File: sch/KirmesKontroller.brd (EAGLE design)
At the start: 100 x 80 mm, 24 parts, among them IC1 R-78E05-1.0, IC2 YB-ESP32-S3-AMP-V2, IC3 ULN2803, J1 MPE 087-1-003, X2 DG240 2,54-8, X4 DG240 2,54-8, X5 DG240 2,54-2, X6 DG240 2,54-2

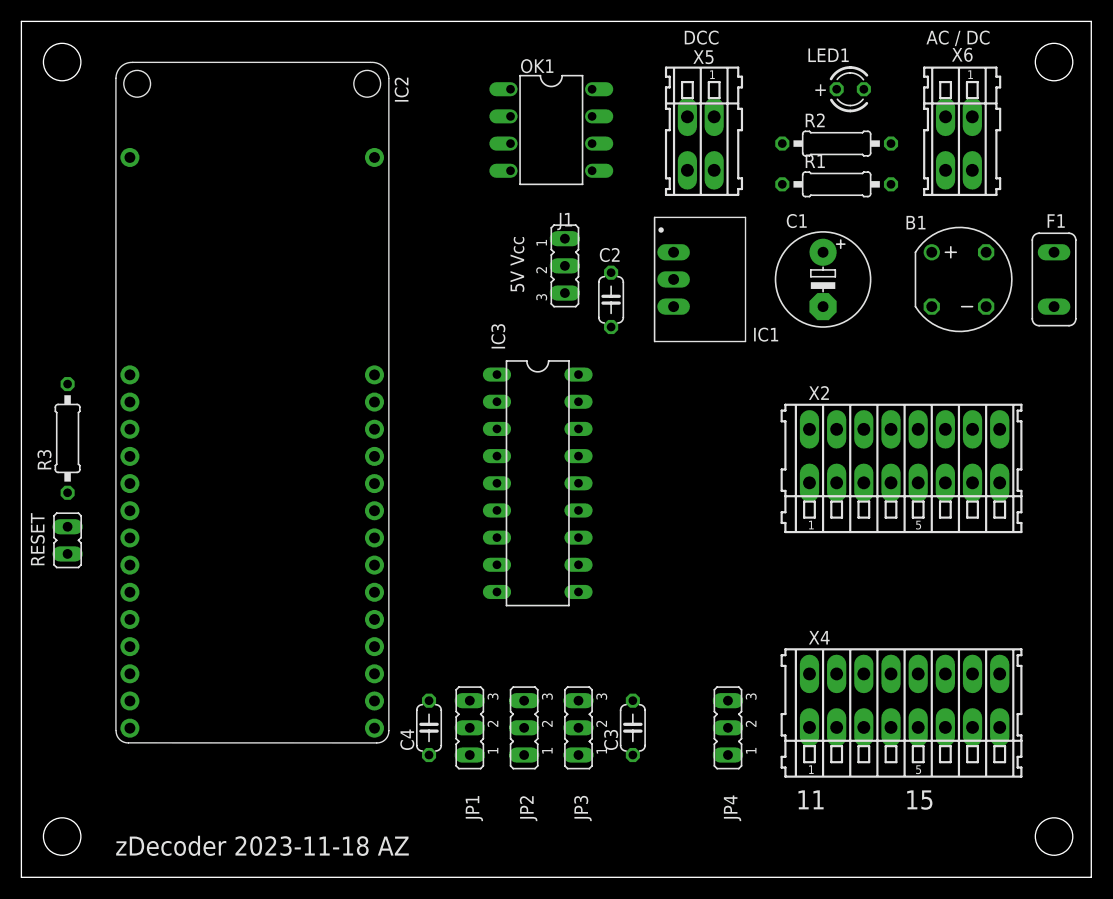
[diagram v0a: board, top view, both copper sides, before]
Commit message: fix: indexes changed
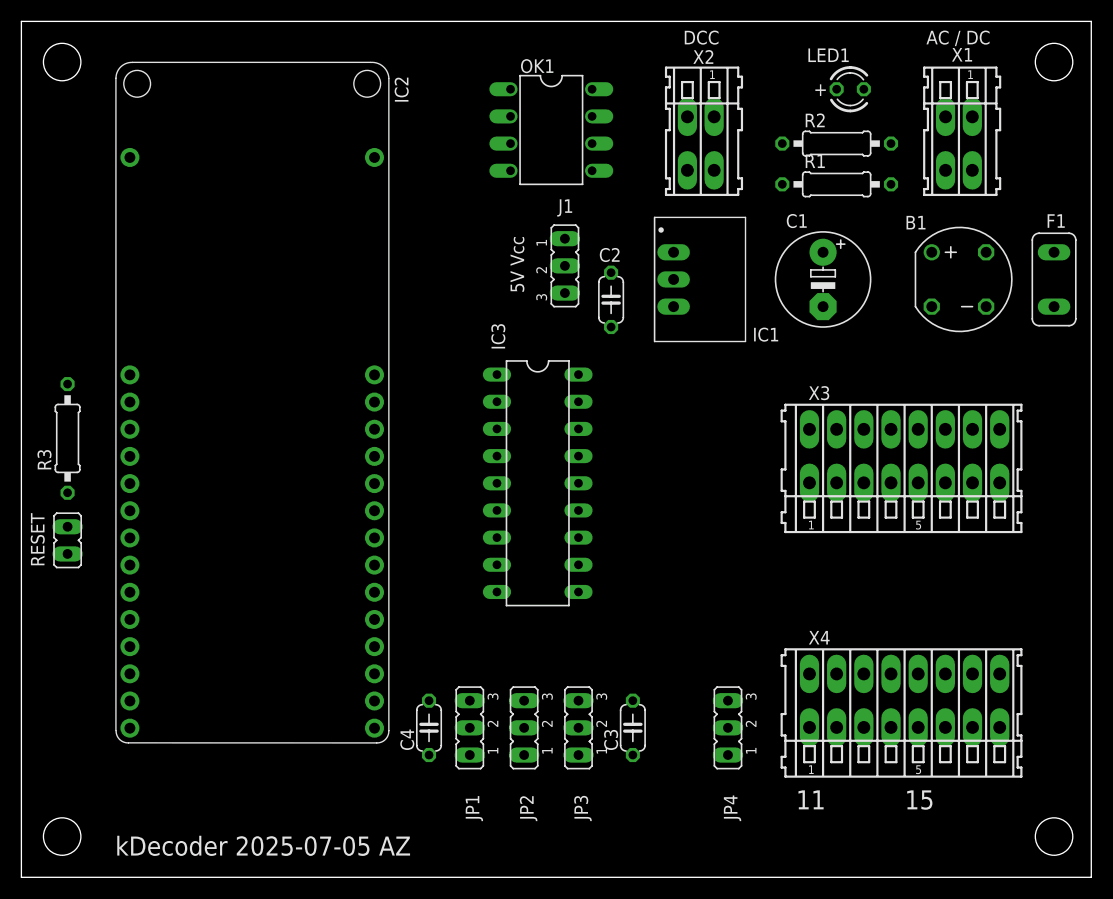
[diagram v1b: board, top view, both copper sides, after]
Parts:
- removed X5: DG240 2,54-2, con-wago255:233-202
- added X3: DG240 2,54-8, con-wago255:233-508
- X2: value DG240 2,54-8 -> DG240 2,54-2; device con-wago255:233-508 -> con-wago255:233-202
- moved X2 34.9 mm to (63.5, 68.6), turned to 180 degrees
- renumbered X6 to X1
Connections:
- net N$11: now also X2.A2; no longer X5.A2
- net N$12: now also X3.A4; no longer X2.A4
- net N$13: now also X3.A3; no longer X2.A3
- net N$14: now also X3.A2; no longer X2.A2
- net N$2: now also X3.A1; no longer X2.A1
- net N$23: now also X3.A8; no longer X2.A8
- net N$4: now also X3.A7; no longer X2.A7
- net N$7: now also X3.A6; no longer X2.A6
- net N$8: now also X3.A5; no longer X2.A5
- net N$9: now also X2.A1; no longer X5.A1
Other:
- board text added: "kDecoder 2025-07-05 AZ"
- board text removed: "zDecoder 2023-11-18 AZ"
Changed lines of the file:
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@@
 <dimension x1="100" y1="80" x2="0" y2="80" x3="50" y3="83.82" textsize="1.778" layer="1"/>
 <dimension x1="0" y1="80" x2="0" y2="0" x3="-3.81" y3="40" textsize="1.778" layer="1"/>
-<text x="8.763" y="2.032" size="1.778" layer="25">zDecoder 2023-11-18 AZ</text>
+<text x="8.763" y="2.032" size="1.778" layer="25">kDecoder 2025-07-05 AZ</text>
 <text x="46.99" y="57.15" size="1.27" layer="25" rot="R90">Vcc</text>
 <text x="46.99" y="54.61" size="1.27" layer="25" rot="R90">5V</text>
@@
 <attribute name="VALUE" x="73.9394" y="67.945" size="1.27" layer="27" ratio="10"/>
 </element>
-<element name="X2" library="con-wago255" library_urn="urn:adsk.eagle:library:198" package="233-508" package3d_urn="urn:adsk.eagle:package:10938/1" value="DG240 2,54-8" x="82.55" y="39.37" smashed="yes">
+<element name="X3" library="con-wago255" library_urn="urn:adsk.eagle:library:198" package="233-508" package3d_urn="urn:adsk.eagle:package:10938/1" value="DG240 2,54-8" x="82.55" y="39.37" smashed="yes">
 <attribute name="MF" value="Wago Corporation" x="106.68" y="-20.32" size="1.778" layer="27" display="off"/>
 <attribute name="MPN" value="0233-0508" x="106.68" y="-20.32" size="1.778" layer="27" display="off"/>
@@
 <attribute name="VALUE" x="82.81" y="21.76" size="1.27" layer="27"/>
 </element>
-<element name="X5" library="con-wago255" library_urn="urn:adsk.eagle:library:198" package="233-202" package3d_urn="urn:adsk.eagle:package:10884/1" value="DG240 2,54-2" x="63.5" y="68.58" smashed="yes" rot="R180">
+<element name="X2" library="con-wago255" library_urn="urn:adsk.eagle:library:198" package="233-202" package3d_urn="urn:adsk.eagle:package:10884/1" value="DG240 2,54-2" x="63.5" y="68.58" smashed="yes" rot="R180">
 <attribute name="MF" value="" x="24.13" y="143.51" size="1.778" layer="27" rot="R180" display="off"/>
 <attribute name="MPN" value="233-202" x="24.13" y="143.51" size="1.778" layer="27" rot="R180" display="off"/>
@@
 <attribute name="VALUE" x="58.75" y="73.18" size="1.27" layer="27" rot="R270"/>
 </element>
-<element name="X6" library="con-wago255" library_urn="urn:adsk.eagle:library:198" package="233-202" package3d_urn="urn:adsk.eagle:package:10884/1" value="DG240 2,54-2" x="87.63" y="68.58" smashed="yes" rot="R180">
+<element name="X1" library="con-wago255" library_urn="urn:adsk.eagle:library:198" package="233-202" package3d_urn="urn:adsk.eagle:package:10884/1" value="DG240 2,54-2" x="87.63" y="68.58" smashed="yes" rot="R180">
 <attribute name="MF" value="" x="40.64" y="143.51" size="1.778" layer="27" rot="R180" display="off"/>
 <attribute name="MPN" value="233-202" x="40.64" y="143.51" size="1.778" layer="27" rot="R180" display="off"/>
@@
 </element>
 <element name="J1" library="jumper" library_urn="urn:adsk.eagle:library:252" package="JP2" package3d_urn="urn:adsk.eagle:package:15452/1" value="MPE 087-1-003" x="50.8" y="57.15" smashed="yes" rot="R270">
-<attribute name="NAME" x="50.165" y="60.833" size="1.27" layer="25" ratio="10"/>
+<attribute name="NAME" x="50.165" y="62.103" size="1.27" layer="25" ratio="10"/>
 <attribute name="POPULARITY" value="34" x="50.8" y="57.15" size="1.778" layer="27" rot="R270" display="off"/>
 <attribute name="VALUE" x="50.8" y="55.2501" size="0.02" layer="27" rot="R270"/>
@@
 <signal name="N$6">
 <contactref element="B1" pad="AC2"/>
-<contactref element="X6" pad="A2"/>
+<contactref element="X1" pad="A2"/>
 <wire x1="85.09" y1="53.34" x2="86.38" y2="66.08" width="0" layer="19" extent="1-1"/>
 </signal>
 <signal name="N$9">
 <contactref element="R2" pad="1"/>
-<contactref element="X5" pad="A1"/>
+<contactref element="X2" pad="A1"/>
 <wire x1="64.75" y1="66.08" x2="71.12" y2="68.58" width="0" layer="19" extent="1-1"/>
 </signal>
@@
 <signal name="N$11">
 <contactref element="OK1" pad="3"/>
-<contactref element="X5" pad="A2"/>
+<contactref element="X2" pad="A2"/>
 <wire x1="45.72" y1="68.58" x2="62.25" y2="66.08" width="0" layer="19" extent="1-1"/>
 </signal>
@@
 <signal name="N$23">
 <contactref element="IC3" pad="11"/>
-<contactref element="X2" pad="A8"/>
+<contactref element="X3" pad="A8"/>
 <wire x1="52.07" y1="29.21" x2="91.44" y2="41.87" width="0" layer="19" extent="1-1"/>
 </signal>
@@
 </signal>
 <signal name="N$15">
-<contactref element="X6" pad="A1"/>
+<contactref element="X1" pad="A1"/>
 <contactref element="F1" pad="1"/>
 <wire x1="88.88" y1="66.08" x2="96.52" y2="58.42" width="0" layer="19" extent="1-1"/>
@@
 <signal name="N$2">
 <contactref element="IC3" pad="18"/>
-<contactref element="X2" pad="A1"/>
+<contactref element="X3" pad="A1"/>
 <wire x1="52.07" y1="46.99" x2="73.66" y2="41.87" width="0" layer="19" extent="1-1"/>
 </signal>
 <signal name="N$4">
 <contactref element="IC3" pad="12"/>
-<contactref element="X2" pad="A7"/>
+<contactref element="X3" pad="A7"/>
 <wire x1="52.07" y1="31.75" x2="88.9" y2="41.87" width="0" layer="19" extent="1-1"/>
 </signal>
 <signal name="N$7">
 <contactref element="IC3" pad="13"/>
-<contactref element="X2" pad="A6"/>
+<contactref element="X3" pad="A6"/>
 <wire x1="52.07" y1="34.29" x2="86.36" y2="41.87" width="0" layer="19" extent="1-1"/>
 </signal>
 <signal name="N$8">
 <contactref element="IC3" pad="14"/>
-<contactref element="X2" pad="A5"/>
+<contactref element="X3" pad="A5"/>
 <wire x1="52.07" y1="36.83" x2="83.82" y2="41.87" width="0" layer="19" extent="1-1"/>
 </signal>
 <signal name="N$12">
 <contactref element="IC3" pad="15"/>
-<contactref element="X2" pad="A4"/>
+<contactref element="X3" pad="A4"/>
 <wire x1="52.07" y1="39.37" x2="81.28" y2="41.87" width="0" layer="19" extent="1-1"/>
 </signal>
 <signal name="N$13">
 <contactref element="IC3" pad="16"/>
-<contactref element="X2" pad="A3"/>
+<contactref element="X3" pad="A3"/>
 <wire x1="52.07" y1="41.91" x2="78.74" y2="41.87" width="0" layer="19" extent="1-1"/>
 </signal>
 <signal name="N$14">
 <contactref element="IC3" pad="17"/>
-<contactref element="X2" pad="A2"/>
+<contactref element="X3" pad="A2"/>
 <wire x1="52.07" y1="44.45" x2="76.2" y2="41.87" width="0" layer="19" extent="1-1"/>
 </signal>

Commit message: initial upload
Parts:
- removed JP1, JP2, JP3, JP4: (no value), jumper:JP2
- added R4, R5: 10k, rcl:0207/10
- added X5, X6, X7, X8: 22-23-2031, con-molex:22-23-2031
- C3, C4: value (none) -> 100n
- moved R3 12.2 mm to (16.5, 41.9)
- moved C3 3.81 mm to (61.0, 14.0), turned to 270 degrees
- moved X3 1.80 mm to (81.3, 40.6)
- turned C4 to 270 degrees
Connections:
- net GPIO39 renamed RESET
- removed net 5V: IC2.5V@1
- removed net GPIO2: IC2.2, OK1.6
- removed net N$12: IC3.15, X3.A4
- removed net N$13: IC3.16, X3.A3
- removed net N$14: IC3.17, X3.A2
- removed net N$17: C3.2, C4.2, JP1.3, JP2.3, JP3.3, JP4.1
- removed net N$2: IC3.18, X3.A1
- removed net N$23: IC3.11, X3.A8
- removed net N$4: IC3.12, X3.A7
- removed net N$7: IC3.13, X3.A6
- removed net N$8: IC3.14, X3.A5
- new net DCC: IC2.40, OK1.6
- new net X3_B-1: IC3.18, X3.A1, X3.B1
- new net X3_B-2: IC3.17, X3.A2, X3.B2
- new net X3_B-3: IC3.16, X3.A3, X3.B3
- new net X3_B-4: IC3.15, X3.A4, X3.B4
- new net X3_B-5: IC3.14, X3.A5, X3.B5
- new net X3_B-6: IC3.13, X3.A6, X3.B6
- new net X3_B-7: IC3.12, X3.A7, X3.B7
- new net X3_B-8: IC3.11, X3.A8, X3.B8
- net +3V3: now also R4.2, R5.2
- net +5V: now also IC2.5V@1, X5.2, X6.2, X7.2; no longer JP1.2, JP2.2, JP3.2
- net GND: now also C3.2, C4.2, X5.3, X6.3, X7.3, X8.3
- net INPUT1: now also IC2.47, R5.1, X8.1; no longer IC2.48, JP4.2
- net INPUT2: now also IC2.48, R4.1, X8.2; no longer IC2.47, JP4.3
- net O21: now also IC2.2, X5.1; no longer IC2.42, JP1.1
- net O22: now also IC2.42, X6.1; no longer IC2.41, JP2.1
- net O23: now also IC2.41, X7.1; no longer IC2.40, JP3.1
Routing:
- net GND: track 0.00 -> 292.1 mm
- net +5V: track 0.00 -> 193.8 mm
- net +3V3: track 0.00 -> 96.3 mm
- net V+: track 0.00 -> 82.4 mm
- net INPUT2: track 0.00 -> 68.6 mm
- net INPUT1: track 0.00 -> 68.5 mm
- net DCC: track 0.00 -> 58.5 mm
- net X3_B-8: track 0.00 -> 53.8 mm
- net O23: track 0.00 -> 51.0 mm
- net VCC: track 0.00 -> 50.6 mm
- net X3_B-7: track 0.00 -> 50.5 mm
- net X3_B-6: track 0.00 -> 47.3 mm
- net N$10: track 0.00 -> 45.6 mm
- net X3_B-5: track 0.00 -> 44.0 mm
- net O22: track 0.00 -> 43.7 mm
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
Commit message: Version 1.0
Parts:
- added C5: 100n, rcl:C050-024X044
- added D1, D2: BAT42, diode:DO35-10
- added R6, R7: 330R, rcl:0207/10
- moved R3 14.5 mm to (20.3, 55.9)
- moved R4 14.5 mm to (24.1, 55.9)
- moved R5 14.5 mm to (27.9, 55.9)
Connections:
- new net N$1: R5.1, R6.2, X8.1
- new net N$2: R4.1, R7.2, X8.2
- net +5V: now also C5.1
- net GND: now also C5.2, D1.A, D2.A
- net INPUT1: now also D1.C, R6.1; no longer R5.1, X8.1
- net INPUT2: now also D2.C, R7.1; no longer R4.1, X8.2
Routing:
- net N$2: track 0.00 -> 61.6 mm
- net N$1: track 0.00 -> 57.5 mm
- net INPUT2: track 68.6 -> 20.7 mm
- net INPUT1: track 68.5 -> 25.6 mm
- net GND: track 292.1 -> 329.7 mm
- net RESET: track 13.9 -> 34.8 mm
- net DCC: track 58.5 -> 65.7 mm, vias 0 -> 1
- net X3_B-8: track 53.8 -> 48.2 mm
- net X3_B-7: track 50.5 -> 45.6 mm
- net X3_B-6: track 47.3 -> 43.1 mm
- net X3_B-5: track 44.0 -> 40.6 mm
- net +3V3: track 96.3 -> 93.2 mm
- net +5V: track 193.8 -> 196.9 mm
- net X3_B-4: track 40.7 -> 38.0 mm
- net X3_B-3: track 37.4 -> 35.9 mm
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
